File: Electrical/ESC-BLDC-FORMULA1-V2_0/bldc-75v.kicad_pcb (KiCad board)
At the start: 4 copper layers, 98 x 90 mm, 122 parts, among them J10 CAN, J11 Wheel, J12 MOTB, J13 MOTA, J5 Battery (anti-spark in cable), J6 MOTC, J7 Throttle, J8 Hall, J9 UART, Q1 CSD19532Q5B, Q2 CSD19532Q5B, Q3 CSD19532Q5B, Q4 CSD19532Q5B, Q5 CSD19532Q5B, Q6 CSD19532Q5B, U1 DRV8353RSRGZT, U2 NUCLEO-G474RE, U5 TJA1051T/3, U6 TPS562201

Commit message: ESC V2.0: 60 V safe TVS (SMCJ60A), keep DRV8353 low-side current sensing
- D8 SMCJ54A -> SMCJ60A (C224057): the 54 V part starts conducting at 60 V and would
  overheat on a 60 V battery; SMCJ60A breaks down at 66.7 V min, clamps at 96.8 V
- Current sensing stays low-side with the DRV8353 amplifiers (inline INA240 variant
  kept as tools/optional/v2_sch_inline.py, not applied)
- All parts on the battery line checked for 60 V: FETs 100 V, VDRAIN 100 V,
  DRV buck VIN 95 V, VM from the 12 V buck, caps 100 V

Co-Authored-By: Claude Opus 5.5 <noreply@anthropic.com>
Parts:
- D8: value SMCJ54A -> SMCJ60A

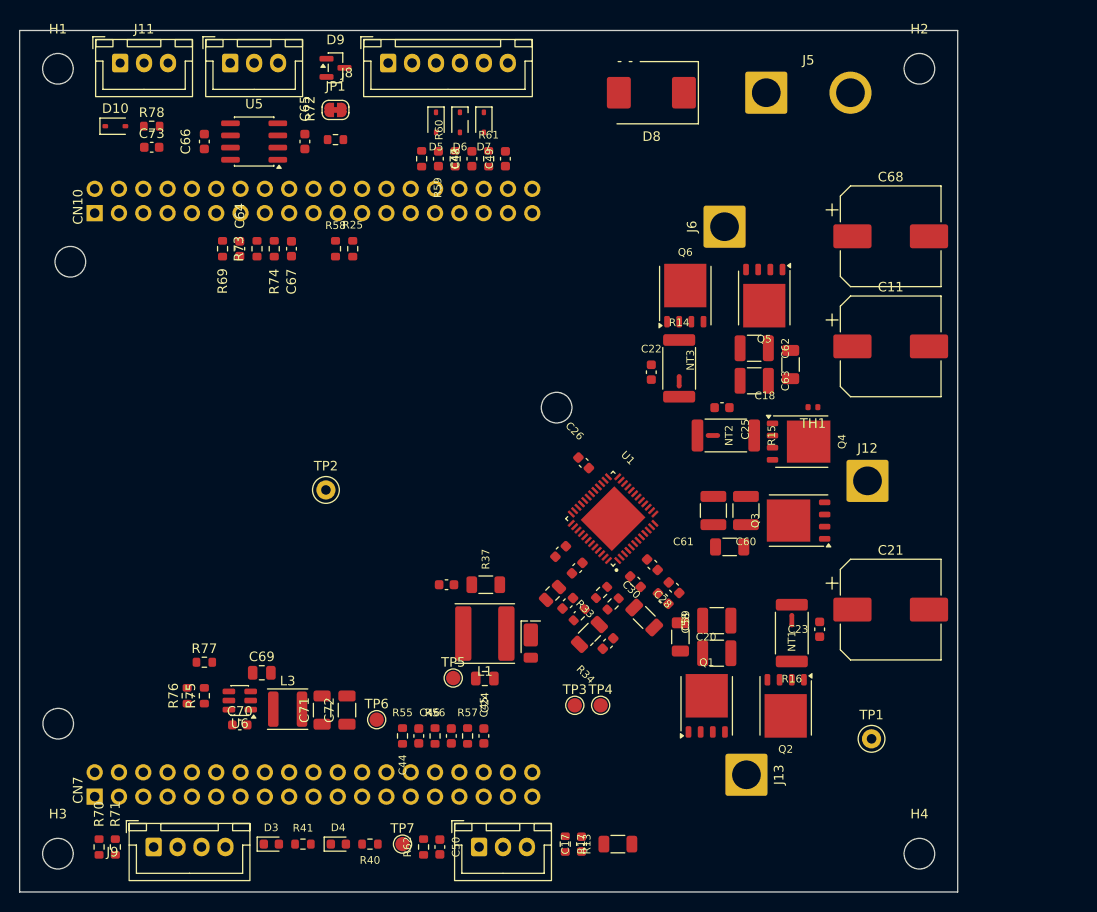
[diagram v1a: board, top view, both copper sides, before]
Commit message: ESC V2.0: big THT bus caps again (3x 330 uF 100 V)
C11/C21/C68: 330 uF 100 V 16x25 mm THT (Samyoung NXA C346987, the V1.2 part, 1.65 A
ripple each = ~5 A) instead of SMD 47 uF 10x10 (too little ripple rating). Placed in
the free corners beside the phase cells, outside the Nucleo area; board 110.5 x 90 mm
(x 143-253.5), right corner holes moved. Parity 0, no courtyard overlaps.

Co-Authored-By: Claude Opus 5.5 <noreply@anthropic.com>
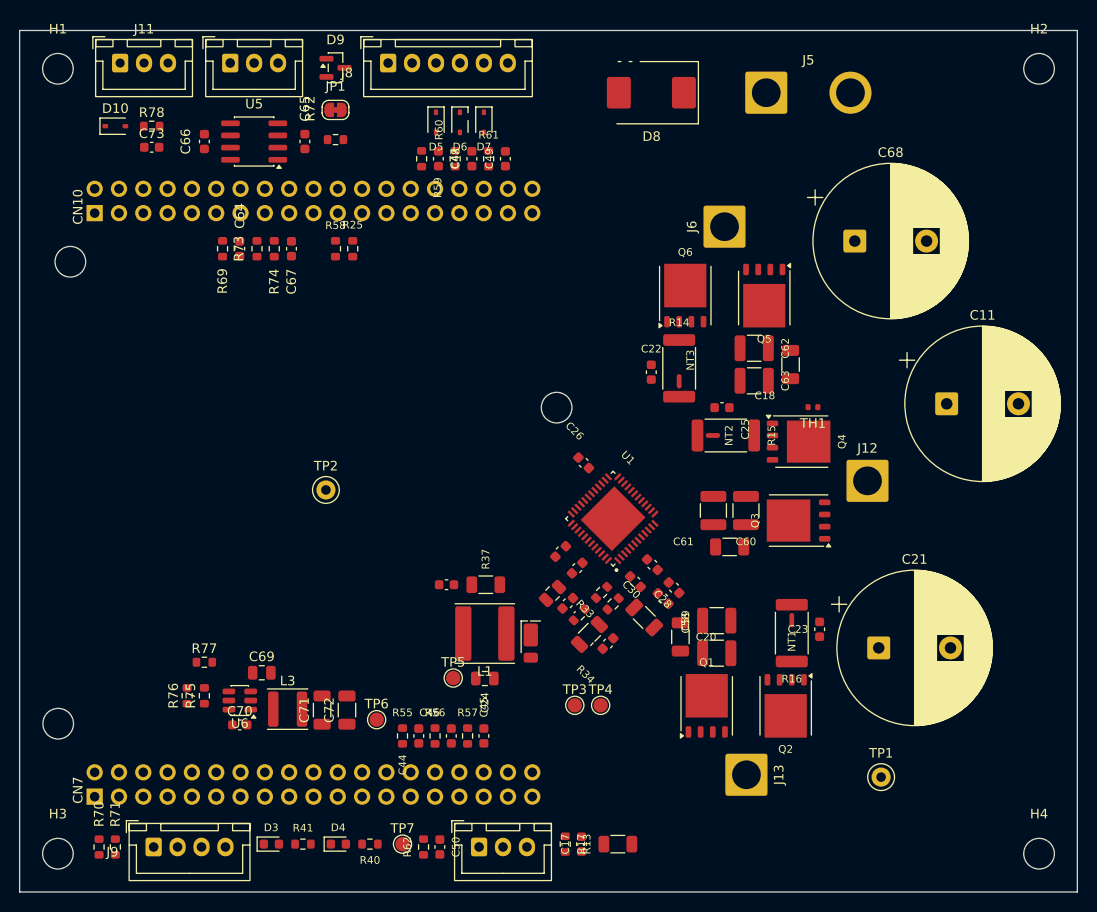
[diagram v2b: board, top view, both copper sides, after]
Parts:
- C11, C21, C68: value 47uF 100V -> 330uF 100V; footprint Capacitor_SMD:CP_Elec_10x10 -> Capacitor_THT:CP_Radial_D16.0mm_P7.50mm
- moved H2 12.5 mm to (249.5, 48.0)
- moved H4 12.5 mm to (249.5, 130.0)
- moved C11 8.38 mm to (239.8, 83.0)
- moved C21 4.19 mm to (232.8, 108.5)
- moved TP1 4.12 mm to (233.0, 122.0)
- moved C68 3.78 mm to (230.2, 66.0)
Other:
- board size 98 x 90 mm -> 110.5 x 90 mm
